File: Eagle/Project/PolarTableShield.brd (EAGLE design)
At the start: 56 x 59.7 mm, 48 parts, among them IC1 74AHC1G86DBV, IC2 LM358D, J1 Pi Power Jack, J10 LED + Radio, J2 Header - Right angled, female, J3 Pi Connection, J5 IR Sensors, J6 Switch A + B, J7 Switch C + D, J8 Switch E + F, Q1 BC337, Q2 2N3906, Q3 BC547, Q4 2N7000, Q5 2N7000, U3 SN74HC595DR

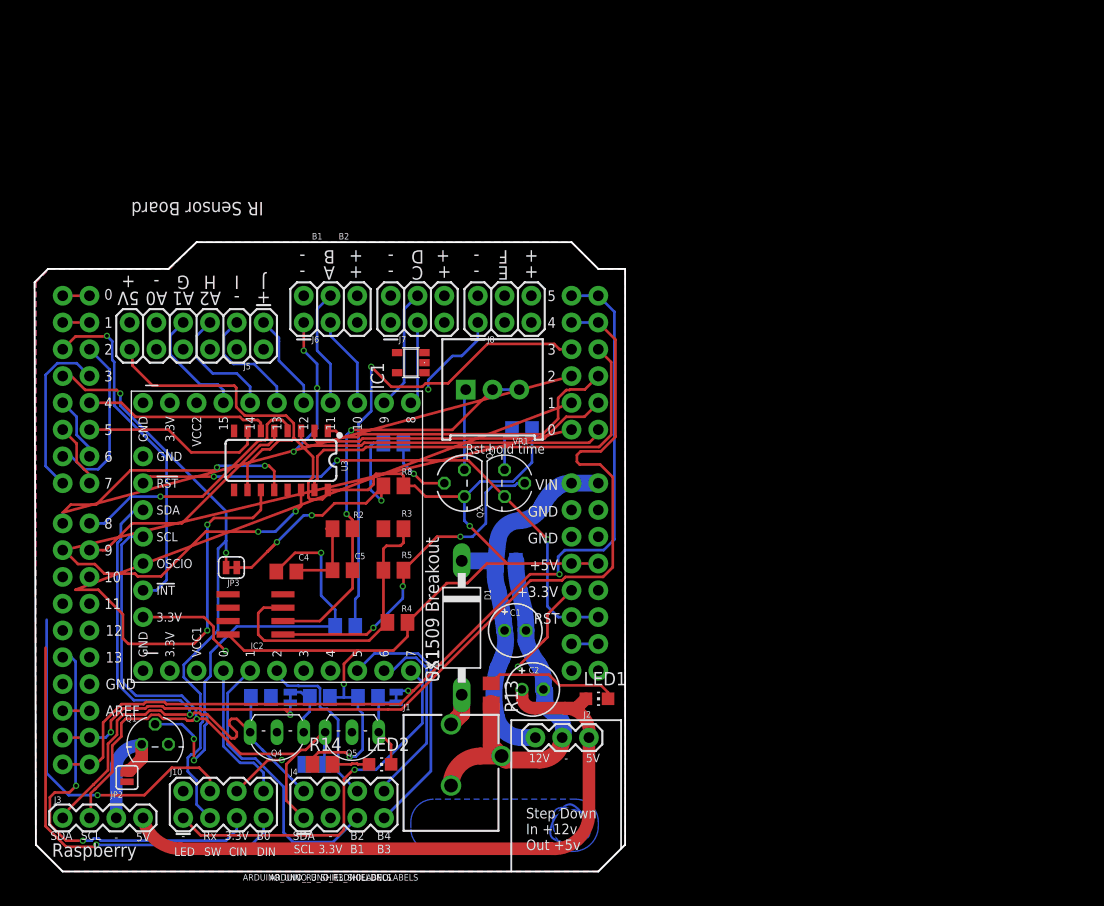
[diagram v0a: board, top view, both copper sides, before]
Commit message: Remove the Arduino headers and just integrated the atmega328 directly
Added atmega328 chip
More indicator lights
Added 3.3v supply
ICP and SPI headers
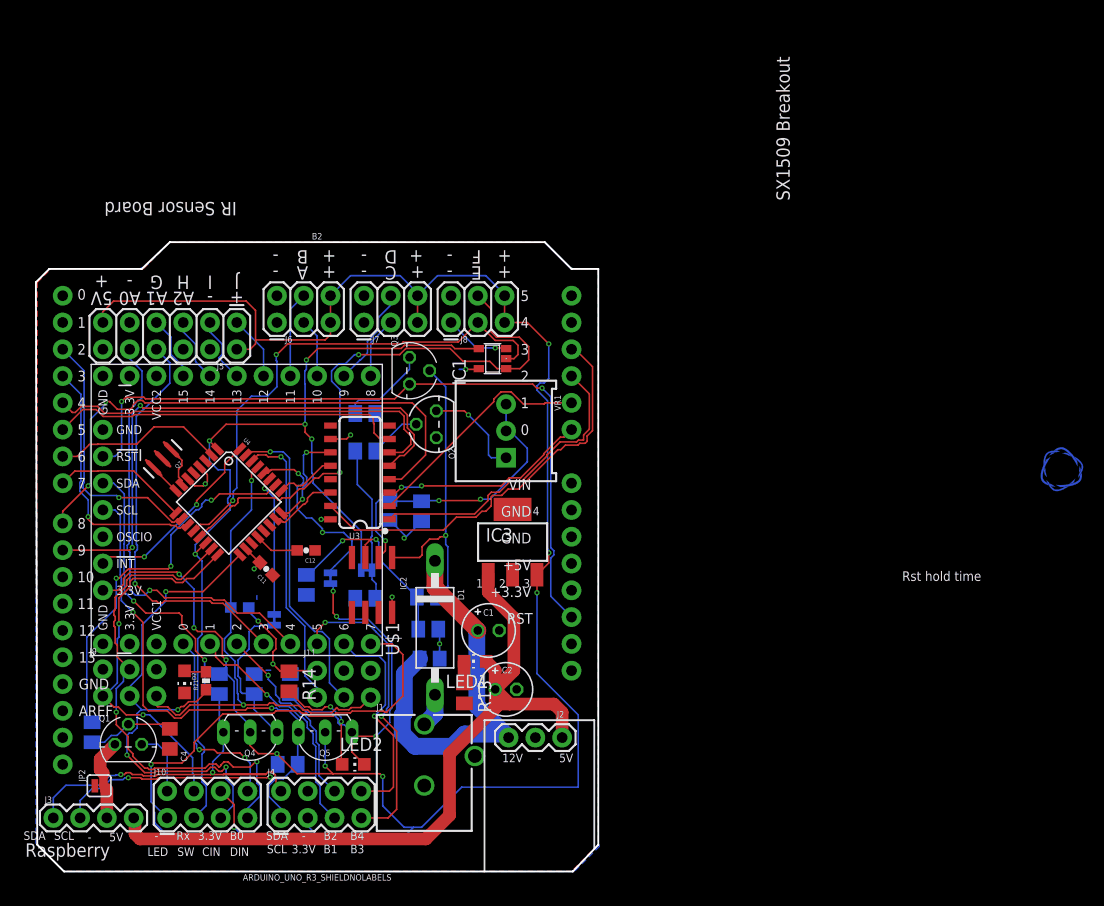
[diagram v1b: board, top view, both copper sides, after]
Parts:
- removed B1: ARDUINO_UNO_R3_SHIELDNOLABELS, keir_library:UNO_R3_SHIELD_NOLABELS
- added C11, C12: 0.1uF, SparkFun:0603-CAP
- added D2: Green, led:CHIP-LED0805
- added IC3: LM340MP-05, linear:SOT223
- added J11: Programmer, keir_library:2X3-NS
- added J9: ISP, keir_library:2X3-NS
- added Q7: 16MHz, Testing:RESONATOR-SMD-1:1
- added R20: 10K, SparkFun:0603-RES
- added R21: 330, SparkFun:0603-RES
- added U4: ATMEGA328, SparkFun:TQFP32-08
- moved U$3 57.6 mm to (97.3, 38.1)
- moved R1 26.0 mm to (5.33, 13.2), turned to 270 degrees
- moved C4 19.3 mm to (12.7, 12.6), turned to 270 degrees
- moved R9 14.9 mm to (31.2, 43.4)
- moved Q3 14.0 mm to (35.4, 47.5)
- moved JP6 12.9 mm to (27.9, 27.8)
- moved JP3 12.8 mm to (31.4, 28.6), flipped to the bottom, turned to 180 degrees
- moved LED1 12.1 mm to (41.7, 19.9), turned to 90 degrees
- moved C9 11.8 mm to (37.3, 20.2)
- moved IC2 11.4 mm to (31.9, 27.2), turned to 180 degrees
- moved R8 11.0 mm to (31.2, 25.9), flipped to the bottom
- moved R3 10.1 mm to (37.2, 23.0), flipped to the bottom
- moved R4 9.34 mm to (25.7, 27.2), flipped to the bottom, turned to 270 degrees
- moved R14 8.49 mm to (24.0, 18.0), turned to 270 degrees
- moved IC1 7.76 mm to (43.3, 48.6)
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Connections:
- removed net 3.3V: B1.3.3V, B2.3.3V, J10.6, J4.3, J5.11, J5.2, J6.5, J6.6, J7.5, J7.6, J8.5, J8.6, Q4.2, Q5.2, R11.1, R12.1, U$1.I1
- removed net 5V: B1.5V, B2.5V, IC2.8, J5.12, Q2.E, R10.1, R14.1, R4.2, R6.1, R8.1, R9.1, U3.10, U3.16
- removed net 5V_SUPPLY: C2.+, J2.3, J3.1, LED1.A
- removed net N$6: C1.-, C2.-, C9.2, J1.GND, J1.GNDBREAK, J2.2, R13.2
- removed net RX: B1.RX, B2.RX
- removed net RXDATA: B1.D12, J10.4
- removed net SCIN: B1.D13, J10.5
- removed net SDIN: B1.D11, J10.7
- removed net TX: B1.TX, B2.TX
- removed net VCC: IC1.5
- new net A6: U4.19
- new net A7: U4.22
- new net MISO(RXDATA): J10.4, J9.1, U4.16
- new net MOSI(SDIN): J10.7, J9.4, U4.15
- new net N$14: D2.A, R21.2
- new net N$15: Q7.3, U4.8
- new net N$16: Q7.1, U4.7
- new net RESET: J11.5, J9.5, R20.1, U4.29
- new net RXI: J11.1, U4.30
- new net SCK(SCIN): J10.5, J9.3, R21.1, U4.17
- new net TXO: J11.3, U4.31
- new net VCC_1: B2.5V, C11.2, C2.+, IC1.5, IC2.8, IC3.1, J11.2, J2.3, J3.1, J5.12, J9.2, LED1.A, Q2.E, R10.1, R14.1, R20.2, R4.2, R6.1, R8.1, R9.1, U3.10, U3.16, U4.18, U4.4, U4.6
- new net VCC_2: IC3.3, J10.6, J4.3, J5.11, J5.2, J6.5, J6.6, J7.5, J7.6, J8.5, J8.6, Q4.2, Q5.2, R11.1, R12.1, U$1.I1
- net !INT: now also U4.32; no longer B1.D2
- net !RES: no longer B1.RES
- net 12V_SUPPLY: no longer B1.VIN, B2.VIN
- net AREF: now also C12.2, U4.20; no longer B1.AREF, B2.AREF
- net CLK: now also U4.24; no longer B1.A1
- net DATA: now also U4.23; no longer B1.A0
- net GND: now also C1.-, C11.1, C12.1, C2.-, C9.2, D2.C, IC3.4, J1.GND, J1.GNDBREAK, J11.6, J2.2, J9.6, Q7.2, R13.2, U4.21, U4.3, U4.5; no longer B1.GND@0, B1.GND@1, B1.GND@2
- net IOREF: no longer B1.IOREF
- net LATCH: now also U4.25; no longer B1.A2
- net PIPOWER_SIGNAL: now also U4.26; no longer B1.A3
- net SCL: now also U4.28; no longer B1.A5, B1.SCL, B2.A5, B2.SCL
- net SDA: now also U4.27; no longer B1.A4, B1.SDA, B2.A4, B2.SDA
- net SW_E: now also IC1.2, U4.12; no longer B1.D8, IC1.1
- net SW_F: now also IC1.1, U4.13; no longer B1.D9, IC1.2
- net WAKE_SW: now also U4.1, U4.14; no longer B1.D10, B1.D3
- net XDIR: now also U4.11; no longer B1.D7
- net XSTEP: now also U4.10; no longer B1.D6
- net YDIR: now also U4.9; no longer B1.D5
- net YSTEP: now also U4.2; no longer B1.D4
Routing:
- net VCC_2: track 0.00 -> 214.8 mm, vias 0 -> 10
- net 5V: track 131.8 -> 0.00 mm, vias 3 -> 0
- net VCC_1: track 0.00 -> 98.0 mm, vias 0 -> 8
- net SDA: track 93.2 -> 13.5 mm, vias 2 -> 1
- net CLK: track 84.3 -> 9.65 mm
- net SCL: track 92.4 -> 18.1 mm
- net DATA: track 77.3 -> 6.67 mm, vias 2 -> 0
- net LATCH: track 73.9 -> 5.79 mm, vias 2 -> 0
- net 5V_SUPPLY: track 63.0 -> 0.00 mm
- net SW_F: track 0.00 -> 56.2 mm, vias 0 -> 2
- net SCK(SCIN): track 0.00 -> 49.8 mm, vias 0 -> 4
- net SW_E: track 0.00 -> 48.7 mm, vias 0 -> 2
- net MOSI(SDIN): track 0.00 -> 47.9 mm, vias 0 -> 2
- net RESET: track 0.00 -> 47.8 mm, vias 0 -> 2
- net B4: track 0.00 -> 41.8 mm, vias 0 -> 1
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- added copper zone on layer 16, net VCC_1
- removed copper zone on layer 16, net 3.3V
- removed copper zone on layer 16, net LOGO
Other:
- board size 56 x 59.7 mm -> 53.3 x 59.7 mm
- board text added: "168 / 5V Reg / 16MHz"
- board text added: "168 / 5V Reg / 20MHz"
- board text added: "168V / 3.3V Reg / 8MHz"
- board text added: "Arduino Pro Mini"
- board text added: "Mark back accordingly"
- board text added: "Valid combinations:"
- board text removed: "Step Down In +12v Out +5v"

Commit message: Updates to the interrupt logic
The timer button and the relative encoder signals now OR together.
The relative encoder now has an XORed interrupt  trigger.
Replaced the main diode with something a bit smaller.
Replaced the 3.3v regulator chip.
Added buffers to the encoder signals.
Changed the crystal setup on the atmega chip.
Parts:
- removed D1: 1N5408, keir_library:DO15-12
- removed IC1: 74AHC1G86DBV, 74xx-little-us:SOT23-5
- removed IC3: LM340MP-05, linear:SOT223
- removed Q7: 16MHz, Testing:RESONATOR-SMD-1:1
- added C3, C6: 13pF, SparkFun:0603-CAP
- added D3: (no value), diode:SMB
- added U1: XOR, Texas Instruments - SN74LVC1G58:SOT363_PHILIPS
- added U2: OR, Texas Instruments - SN74LVC1G58:SOT363_PHILIPS
- added U5, U6, U7: Buffer, Texas Instruments - SN74LVC1G58:SOT363_PHILIPS
- added U8: CD74HC4094M96, keir_library:D16
- added Y1: TSX-3225_16.0000MF18X-AC3, keir_library:XTAL_TSX-3225_16.0000MF18X-AC3
- Q3: value BC547 -> 2N3904
- R3: value 22k -> 47k
- R4: value 16.2k -> 3k
- R5: value 221k -> 11k
- R9: value 1k -> 5k
- U3: value SN74HC595DR -> TLV73333PDBVT; device keir_library:SO16 -> keir_library:DBV5
- moved U3 20.6 mm to (47.4, 25.7), turned to 0 degrees
- moved R3 14.2 mm to (25.7, 31.2), turned to 270 degrees
- moved LED1 9.96 mm to (50.8, 16.0), turned to 270 degrees
- moved R9 9.83 mm to (41.0, 42.4), turned to 90 degrees
- moved R13 8.57 mm to (47.2, 22.4), turned to 180 degrees
- moved C5 4.97 mm to (38.5, 34.7), flipped to the top
- moved C9 4.95 mm to (41.0, 16.9), flipped to the top, turned to 0 degrees
- moved R5 4.16 mm to (34.9, 29.6), flipped to the top, turned to 90 degrees
- moved C1 2.70 mm to (41.1, 20.8)
- moved C11 2.44 mm to (23.7, 27.2)
- moved U4 1.81 mm to (19.7, 33.9)
- moved C2 1.40 mm to (46.0, 17.4), turned to 180 degrees
- moved C12 0.64 mm to (26.1, 30.1)
- moved R2 0.57 mm to (36.3, 34.7), flipped to the top
- moved IC2 0.38 mm to (31.5, 27.2)
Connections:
- removed net CLK: U3.11, U4.24
- removed net N$15: Q7.3, U4.8
- new net CLOCK: U4.24, U8.3
- new net N$6: R9.1, VR1.1
- new net SW_EF_XOR: U1.4, U2.6
- new net SW_E_BUF: U1.6, U4.12, U6.4
- new net SW_F_BUF: U1.1, U1.3, U4.13, U5.4
- new net SW_OR_ENCODER: U2.4, U4.1
- new net WAKE_SW_BUF: JP3.1, U2.3, U4.14, U7.4
- net 12V_SUPPLY: now also D3.C; no longer D1.C
- net DATA: now also U8.2; no longer U3.14
- net ENX: now also U8.5; no longer U3.1
- net ENY: now also U8.7; no longer U3.3
- net GND: now also C3.2, C6.2, Q3.3, U1.2, U2.1, U2.2, U3.2, U5.1, U5.2, U5.6, U6.1, U6.2, U6.6, U7.1, U7.2, U7.6, U8.8, Y1.2, Y1.4; no longer IC1.3, IC3.4, Q7.2, U3.13, U3.8
- net LATCH: now also U8.1; no longer U3.12
- net N$16: now also C6.1, Y1.3; no longer Q7.1
- net N$3: now also Q2.C; no longer Q3.3
- net N$4: now also D3.A; no longer D1.A
- net N$7: now also C3.1, U4.8, Y1.1; no longer Q2.C, VR1.1
- net SLEEPX: now also U8.4; no longer U3.15
- net SLEEPY: now also U8.6; no longer U3.2
- net SW_E: now also U6.3; no longer IC1.2, U4.12
- net SW_F: now also U5.3; no longer IC1.1, U4.13
- net VCC_1: now also U1.5, U2.5, U3.1, U3.3, U5.5, U6.5, U7.5, U8.16; no longer IC1.5, IC3.1, R9.1, U3.10, U3.16
- net VCC_2: now also B2.3.3V, U3.5; no longer IC3.3
- net WAKE_SW: now also U7.3; no longer IC1.4, JP3.1, U4.1, U4.14
- net XMS1: now also U8.12; no longer U3.6
- net XMS2: now also U8.11; no longer U3.7
- net YMS1: now also U8.14; no longer U3.4
- net YMS2: now also U8.13; no longer U3.5
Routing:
- net WAKE_SW: track 91.9 -> 8.25 mm, vias 5 -> 1
- net SW_F: track 56.2 -> 5.46 mm, vias 2 -> 0
- net SW_E: track 48.7 -> 2.39 mm, vias 2 -> 0
- net SW_F_BUF: track 0.00 -> 44.2 mm, vias 0 -> 6
- net SW_E_BUF: track 0.00 -> 41.3 mm, vias 0 -> 3
- net WAKE_SW_BUF: track 0.00 -> 40.8 mm, vias 0 -> 4
- net VCC_2: track 214.8 -> 240.2 mm
- net 12V_SUPPLY: track 38.7 -> 15.1 mm
- net SW_EF_XOR: track 0.00 -> 21.9 mm, vias 0 -> 4
- net VCC_1: track 98.0 -> 114.9 mm, vias 8 -> 10
- net !INT: track 18.2 -> 33.9 mm, vias 2 -> 1
- net SW_OR_ENCODER: track 0.00 -> 14.6 mm, vias 0 -> 2
- net GND: track 20.2 -> 7.81 mm, vias 3 -> 1
- net CLOCK: track 0.00 -> 10.5 mm
- net CLK: track 9.65 -> 0.00 mm, vias 2 -> 0
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
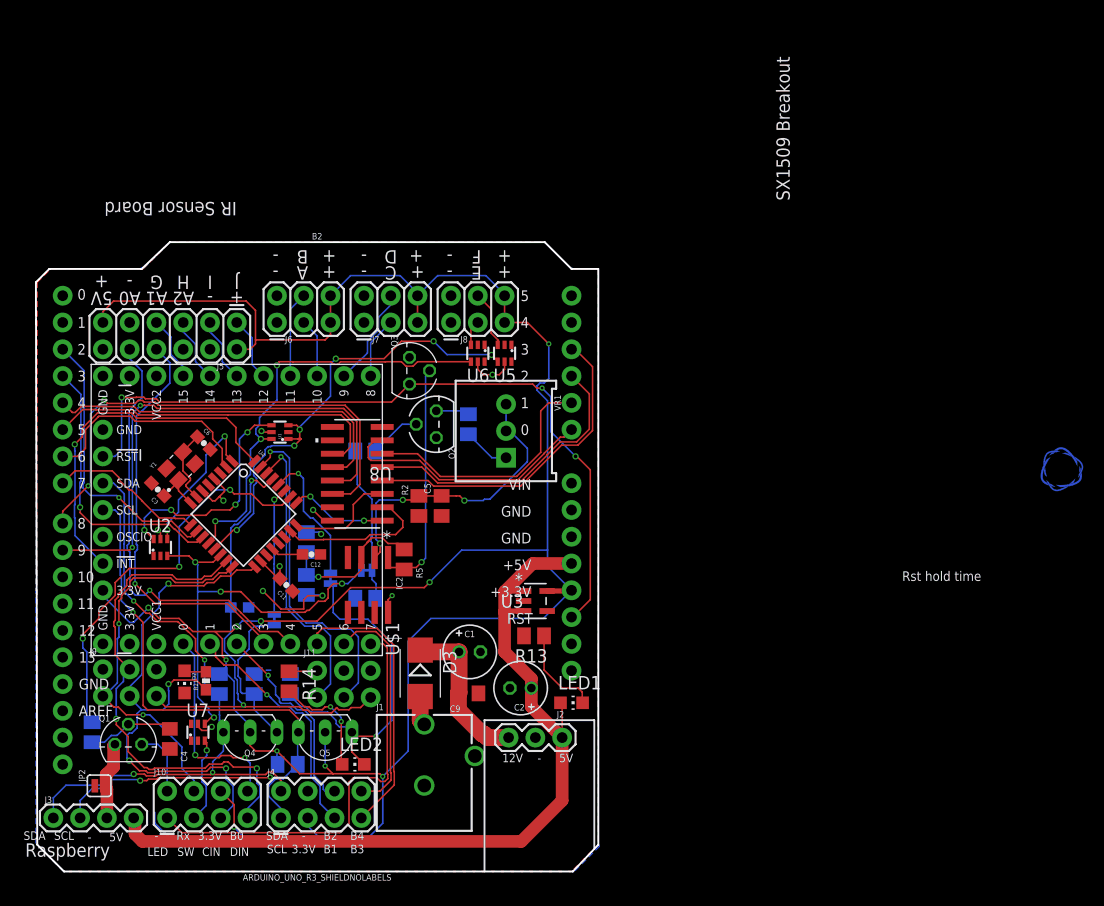
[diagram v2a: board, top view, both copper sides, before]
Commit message: Thinking about splitting out the power into a separate board.
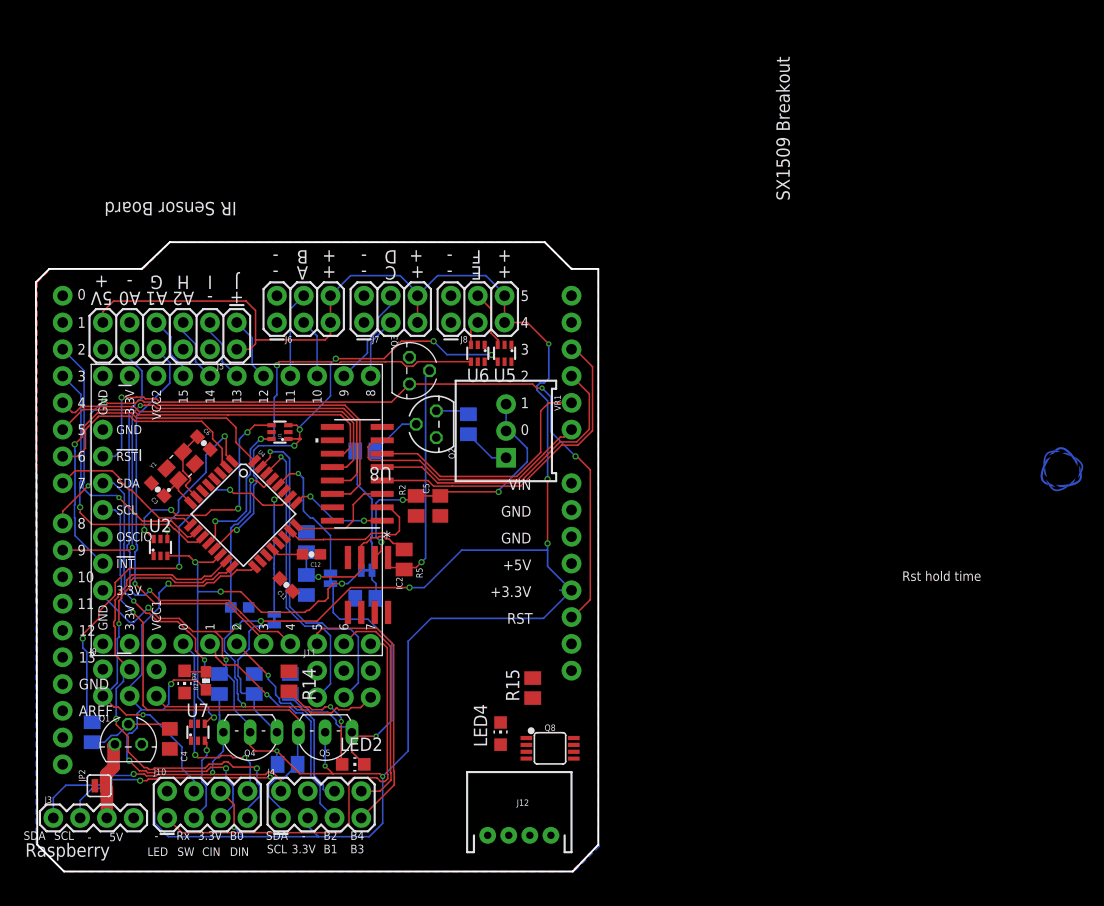
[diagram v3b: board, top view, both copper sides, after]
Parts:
- removed C1, C2: 100u, rcl:E2-5
- removed C9: 100n, rcl:C0805
- removed D3: (no value), diode:SMB
- removed J1: Pi Power Jack, SparkFun-Connectors:POWER_JACK_PTH_BREAD
- removed J2: Header - Right angled, female, keir_library:1X03
- removed LED1: (no value), led:CHIP-LED0805
- removed R13: 1k, rcl:M0805
- removed U3: TLV73333PDBVT, keir_library:DBV5
- added J12: (no value), SparkFun-Connectors:JST-4-PTH
- added LED4: (no value), led:CHIP-LED0805
- added Q8: IRF7509, SparkFun-DiscreteSemi:MSOP8
- added R15: 1k, rcl:M0805
- moved R2 0.25 mm to (36.1, 34.7)
- moved C5 0.13 mm to (38.4, 34.7)
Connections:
- net 12V_SUPPLY: now also J12.3; no longer C1.+, C9.1, D3.C, J2.1
- net GND: now also Q8.1, R15.1; no longer C1.-, C2.-, C9.2, J1.GND, J1.GNDBREAK, J2.2, R13.2, U3.2
- net N$4: now also J12.4, Q8.7, Q8.8; no longer D3.A, J1.PWR
- net N$9: now also LED4.C, R15.2; no longer LED1.C, R13.1
- net VCC_1: now also J12.2, LED4.A, Q8.2; no longer C2.+, J2.3, LED1.A, U3.1, U3.3
- net VCC_2: now also J12.1; no longer U3.5
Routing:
- net VCC_1: track 114.9 -> 0.00 mm, vias 10 -> 0
- net 12V_SUPPLY: track 15.1 -> 0.00 mm
- net N$9: track 8.76 -> 0.00 mm
- net GND: track 7.81 -> 0.00 mm, vias 1 -> 0
- net N$4: track 2.80 -> 0.00 mm
- net VCC_2: track 240.2 -> 238.5 mm, vias 10 -> 12
- net SW_F_BUF: track 44.2 -> 44.8 mm
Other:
- board text removed: "12V"

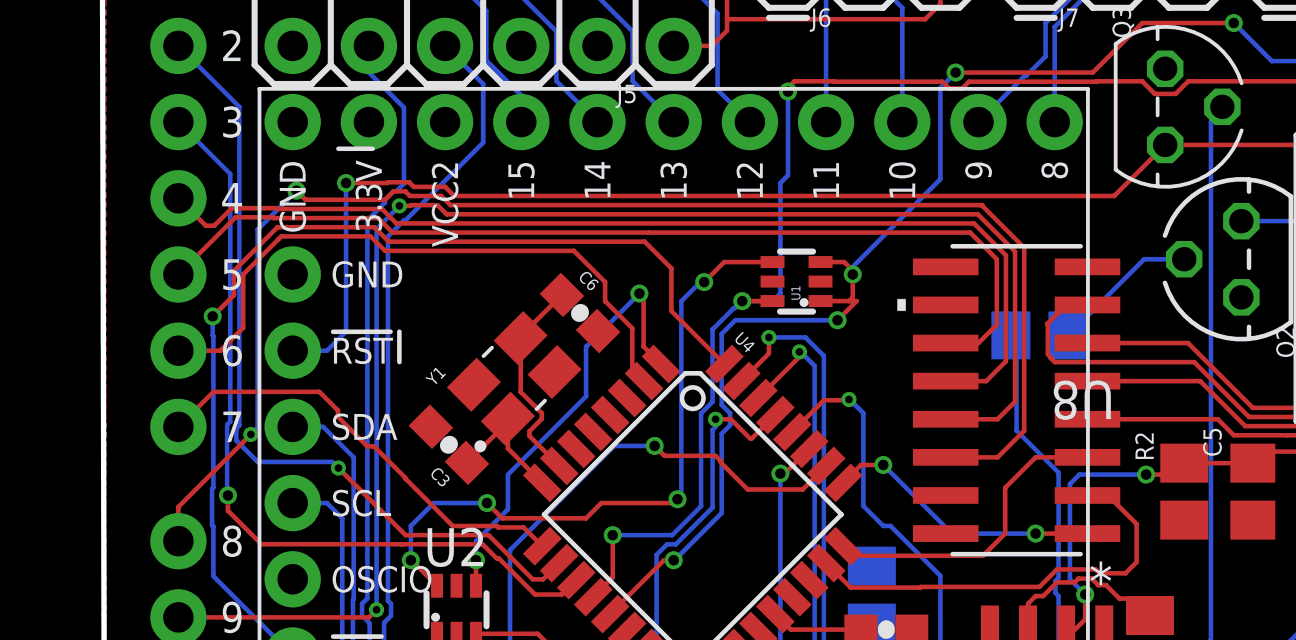
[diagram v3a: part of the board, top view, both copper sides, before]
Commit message: Updated motor setting pins to match code.
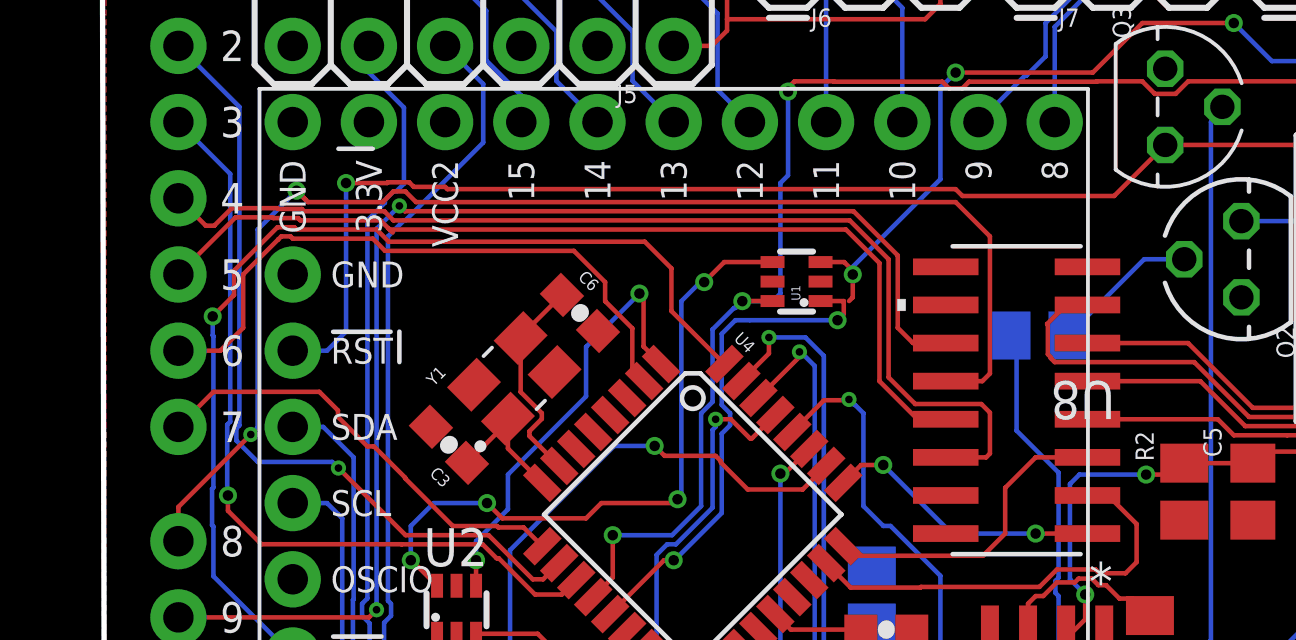
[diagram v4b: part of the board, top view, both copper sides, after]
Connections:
- net XMS1: now also U8.14; no longer U8.12
- net XMS2: now also U8.13; no longer U8.11
- net YMS1: now also U8.12; no longer U8.14
- net YMS2: now also U8.11; no longer U8.13
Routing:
- net YMS2: track 49.2 -> 42.0 mm
- net YMS1: track 47.7 -> 43.9 mm
- net XMS2: track 32.8 -> 31.7 mm
- net XMS1: track 34.7 -> 35.7 mm
- net SW_F_BUF: track 44.8 -> 44.2 mm
